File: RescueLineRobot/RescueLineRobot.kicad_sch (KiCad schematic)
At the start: 18 parts

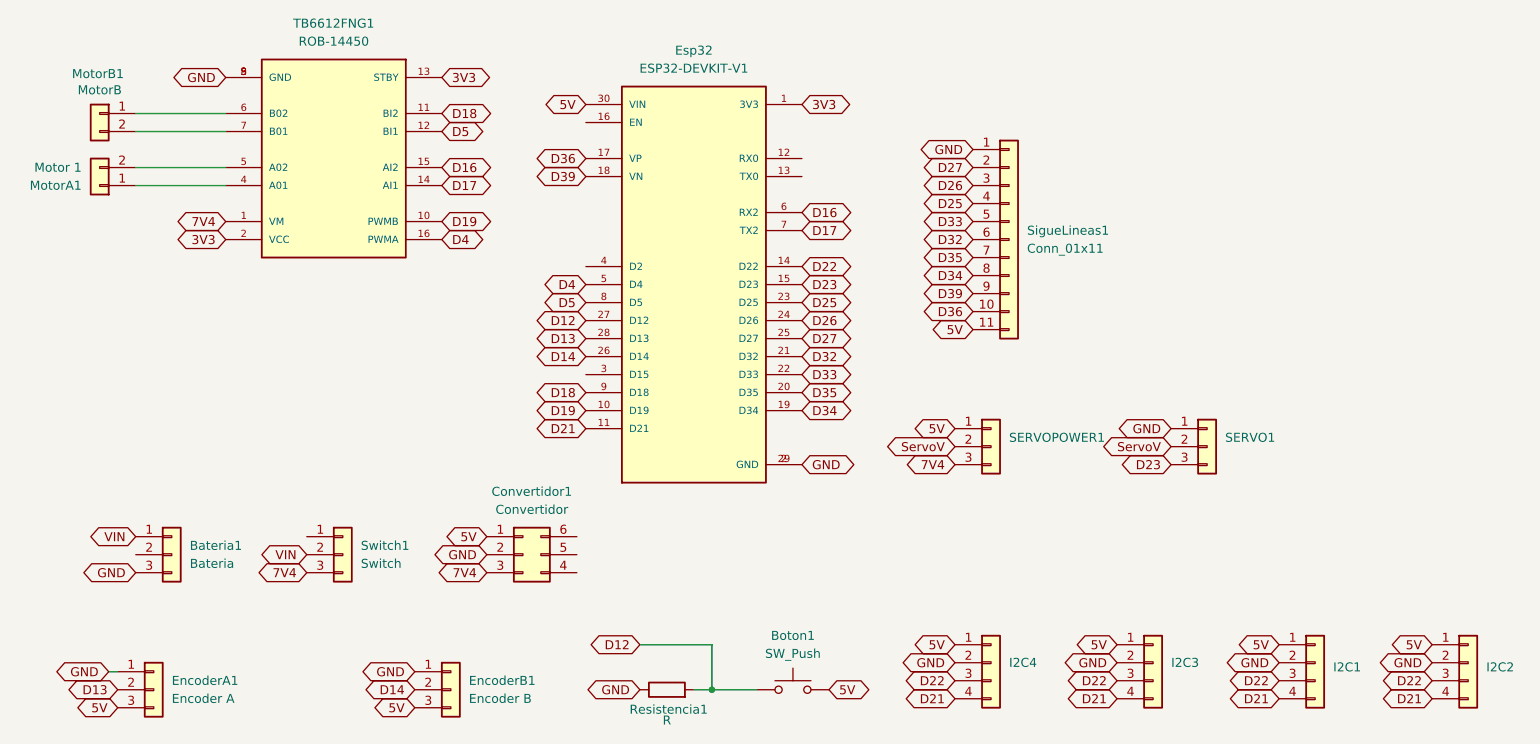
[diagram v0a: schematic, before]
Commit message: Cambio giroscopio
Se cambio el sistema de acople del giroscopio para que sea igual al del conversor de voltaje
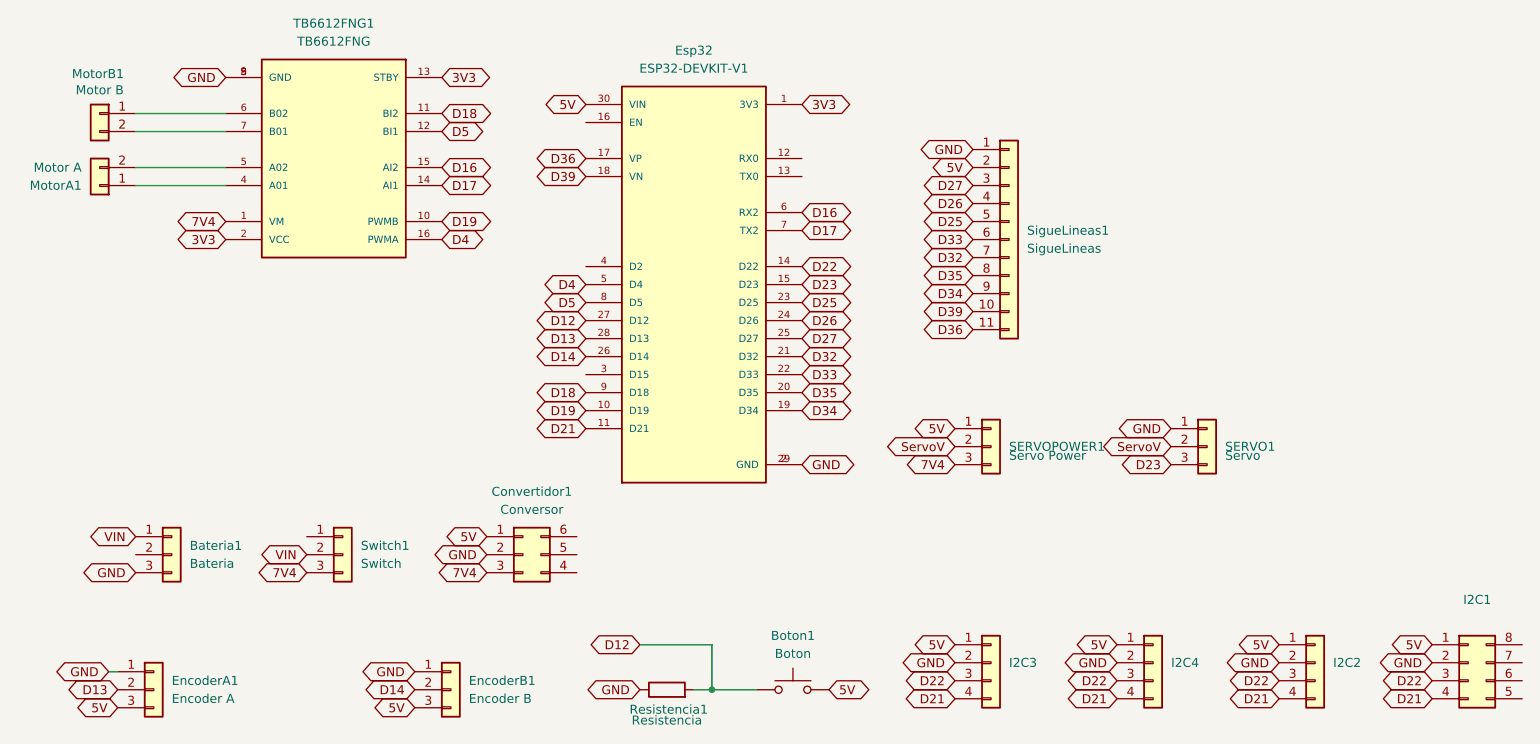
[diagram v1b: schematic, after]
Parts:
- Boton1: value SW_Push -> Boton
- Convertidor1: value Convertidor -> Conversor
- I2C1: renamed from I2C2; symbol Connector_Generic:Conn_01x04 -> Connector_Generic:Conn_02x04_Counter_Clockwise
- MotorA1: value Motor 1 -> Motor A
- MotorB1: value MotorB -> Motor B
- Resistencia1: value R -> Resistencia
- SERVO1: value Conn_01x03 -> Servo
- SERVOPOWER1: value Conn_01x03 -> Servo Power
- SigueLineas1: value Conn_01x11 -> SigueLineas
- TB6612FNG1: value ROB-14450 -> TB6612FNG
- renumbered I2C1 to I2C2, I2C4 to I2C3, I2C3 to I2C4
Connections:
- net 5V: now also SigueLineas1.2 (Pin_2); no longer SigueLineas1.11 (Pin_11)
- net D25: now also SigueLineas1.5 (Pin_5); no longer SigueLineas1.4 (Pin_4)
- net D26: now also SigueLineas1.4 (Pin_4); no longer SigueLineas1.3 (Pin_3)
- net D27: now also SigueLineas1.3 (Pin_3); no longer SigueLineas1.2 (Pin_2)
- net D32: now also SigueLineas1.7 (Pin_7); no longer SigueLineas1.6 (Pin_6)
- net D33: now also SigueLineas1.6 (Pin_6); no longer SigueLineas1.5 (Pin_5)
- net D34: now also SigueLineas1.9 (Pin_9); no longer SigueLineas1.8 (Pin_8)
- net D35: now also SigueLineas1.8 (Pin_8); no longer SigueLineas1.7 (Pin_7)
- net D36: now also SigueLineas1.11 (Pin_11); no longer SigueLineas1.10 (Pin_10)
- net D39: now also SigueLineas1.10 (Pin_10); no longer SigueLineas1.9 (Pin_9)
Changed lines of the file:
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@@
 	(global_label "D25"
 		(shape bidirectional)
-		(at 149.86 44.45 180)
+		(at 149.86 46.99 180)
 		(fields_autoplaced yes)
 		(effects
@@
 		)
 		(property "Intersheetrefs" "${INTERSHEET_REFS}"
-			(at 142.0745 44.45 0)
+			(at 142.0745 46.99 0)
 			(effects
 				(font
@@
 	(global_label "D27"
 		(shape bidirectional)
-		(at 149.86 39.37 180)
+		(at 149.86 41.91 180)
 		(fields_autoplaced yes)
 		(effects
@@
 		)
 		(property "Intersheetrefs" "${INTERSHEET_REFS}"
-			(at 142.0745 39.37 0)
+			(at 142.0745 41.91 0)
 			(effects
 				(font
@@
 	(global_label "D39"
 		(shape bidirectional)
-		(at 149.86 57.15 180)
+		(at 149.86 59.69 180)
 		(fields_autoplaced yes)
 		(effects
@@
 		)
 		(property "Intersheetrefs" "${INTERSHEET_REFS}"
-			(at 142.0745 57.15 0)
+			(at 142.0745 59.69 0)
 			(effects
 				(font
@@
 	(global_label "5V"
 		(shape bidirectional)
-		(at 149.86 62.23 180)
+		(at 149.86 39.37 180)
 		(fields_autoplaced yes)
 		(effects
@@
 		)
 		(property "Intersheetrefs" "${INTERSHEET_REFS}"
-			(at 143.4654 62.23 0)
+			(at 143.4654 39.37 0)
 			(effects
 				(font
@@
 	(global_label "D33"
 		(shape bidirectional)
-		(at 149.86 46.99 180)
+		(at 149.86 49.53 180)
 		(fields_autoplaced yes)
 		(effects
@@
 		)
 		(property "Intersheetrefs" "${INTERSHEET_REFS}"
-			(at 142.0745 46.99 0)
+			(at 142.0745 49.53 0)
 			(effects
 				(font
@@
 	(global_label "D35"
 		(shape bidirectional)
-		(at 149.86 52.07 180)
+		(at 149.86 54.61 180)
 		(fields_autoplaced yes)
 		(effects
@@
 		)
 		(property "Intersheetrefs" "${INTERSHEET_REFS}"
-			(at 142.0745 52.07 0)
+			(at 142.0745 54.61 0)
 			(effects
 				(font
@@
 	(global_label "D32"
 		(shape bidirectional)
-		(at 149.86 49.53 180)
+		(at 149.86 52.07 180)
 		(fields_autoplaced yes)
 		(effects
@@
 		)
 		(property "Intersheetrefs" "${INTERSHEET_REFS}"
-			(at 142.0745 49.53 0)
+			(at 142.0745 52.07 0)
 			(effects
 				(font
@@
 	(global_label "D26"
 		(shape bidirectional)
-		(at 149.86 41.91 180)
+		(at 149.86 44.45 180)
 		(fields_autoplaced yes)
 		(effects
@@
 		)
 		(property "Intersheetrefs" "${INTERSHEET_REFS}"
-			(at 142.0745 41.91 0)
+			(at 142.0745 44.45 0)
 			(effects
 				(font
@@
 	(global_label "D34"
 		(shape bidirectional)
-		(at 149.86 54.61 180)
+		(at 149.86 57.15 180)
 		(fields_autoplaced yes)
 		(effects
@@
 		)
 		(property "Intersheetrefs" "${INTERSHEET_REFS}"
-			(at 142.0745 54.61 0)
+			(at 142.0745 57.15 0)
 			(effects
 				(font
@@
 	(global_label "D36"
 		(shape bidirectional)
-		(at 149.86 59.69 180)
+		(at 149.86 62.23 180)
 		(fields_autoplaced yes)
 		(effects
@@
 		)
 		(property "Intersheetrefs" "${INTERSHEET_REFS}"
-			(at 142.0745 59.69 0)
+			(at 142.0745 62.23 0)
 			(effects
 				(font
@@
 		(fields_autoplaced yes)
 		(property "Reference" "SERVO1"
-			(at 185.42 77.4699 0)
+			(at 185.42 78.7399 0)
 			(effects
 				(font
@@
 			)
 		)
-		(property "Value" "Conn_01x03"
+		(property "Value" "Servo"
 			(at 185.42 80.0099 0)
 			(effects
@@
 				)
 				(justify left)
-				(hide yes)
 			)
 		)
@@
 		(dnp no)
 		(fields_autoplaced yes)
-		(property "Reference" "I2C3"
+		(property "Reference" "I2C4"
 			(at 177.8 109.2199 0)
 			(effects
@@
 			(project "RescueLineRobot"
 				(path "/08dd59d3-3158-43a6-a3e1-925f8e86ce81"
-					(reference "I2C3")
+					(reference "I2C4")
 					(unit 1)
 				)
@@
 			)
 		)
-		(property "Value" "MotorB"
+		(property "Value" "Motor B"
 			(at 26.67 28.448 0)
 			(effects
@@
 		(dnp no)
 		(fields_autoplaced yes)
-		(property "Reference" "I2C4"
+		(property "Reference" "I2C3"
 			(at 154.94 109.2199 0)
 			(effects
@@
 			(project "RescueLineRobot"
 				(path "/08dd59d3-3158-43a6-a3e1-925f8e86ce81"
-					(reference "I2C4")
+					(reference "I2C3")
 					(unit 1)
 				)
@@
 		(dnp no)
 		(fields_autoplaced yes)
-		(property "Reference" "I2C1"
-			(at 200.66 109.8549 0)
+		(property "Reference" "I2C2"
+			(at 200.66 109.2199 0)
 			(effects
 				(font
@@
 		)
 		(property "Value" "~"
-			(at 200.66 111.76 0)
+			(at 200.66 111.7599 0)
 			(effects
 				(font
@@
 			(project "RescueLineRobot"
 				(path "/08dd59d3-3158-43a6-a3e1-925f8e86ce81"
-					(reference "I2C1")
+					(reference "I2C2")
 					(unit 1)
 				)
@@
 			)
 		)
-		(property "Value" "ROB-14450"
+		(property "Value" "TB6612FNG"
 			(at 59.69 21.59 0)
 			(effects
@@
 			)
 		)
-		(property "Value" "SW_Push"
+		(property "Value" "Boton"
 			(at 124.46 107.95 0)
 			(effects
@@
 			)
 		)
-		(property "Value" "Convertidor"
+		(property "Value" "Conversor"
 			(at 87.63 87.63 0)
 			(effects
@@
 	)
 	(symbol
-		(lib_id "Connector_Generic:Conn_01x04")
+		(lib_id "Connector_Generic:Conn_02x04_Counter_Clockwise")
 		(at 219.71 109.22 0)
 		(unit 1)
@@
 		(dnp no)
 		(fields_autoplaced yes)
-		(property "Reference" "I2C2"
-			(at 222.25 109.8549 0)
+		(property "Reference" "I2C1"
+			(at 220.98 100.33 0)
 			(effects
 				(font
 					(size 1.27 1.27)
 				)
-				(justify left)
 			)
 		)
 		(property "Value" "~"
-			(at 222.25 111.76 0)
+			(at 220.98 102.87 0)
 			(effects
 				(font
 					(size 1.27 1.27)
 				)
-				(justify left)
 			)
 		)
@@
 			)
 		)
-		(property "Description" "Generic connector, single row, 01x04, script generated (kicad-library-utils/schlib/autogen/connector/)"
+		(property "Description" "Generic connector, double row, 02x04, counter clockwise pin numbering scheme (similar to DIP package numbering), script generated (kicad-library-utils/schlib/autogen/connector/)"
 			(at 219.71 109.22 0)
 			(effects
@@
 		(pin "4"
 		)
+		(pin "8"
+		)
+		(pin "7"
+		)
+		(pin "6"
+		)
+		(pin "5"
+		)
 		(instances
 			(project "RescueLineRobot"
 				(path "/08dd59d3-3158-43a6-a3e1-925f8e86ce81"
-					(reference "I2C2")
+					(reference "I2C1")
 					(unit 1)
 				)
@@
 			)
 		)
-		(property "Value" "Motor 1"
+		(property "Value" "Motor A"
 			(at 24.13 39.3701 0)
 			(effects
@@
 		(fields_autoplaced yes)
 		(property "Reference" "SERVOPOWER1"
-			(at 154.94 77.4699 0)
+			(at 154.94 78.7399 0)
 			(effects
 				(font
@@
 			)
 		)
-		(property "Value" "Conn_01x03"
+		(property "Value" "Servo Power"
 			(at 154.94 80.0099 0)
 			(effects
@@
 				)
 				(justify left)
-				(hide yes)
 			)
 		)
@@
 			)
 		)
-		(property "Value" "R"
+		(property "Value" "Resistencia"
 			(at 106.68 117.348 90)
 			(effects
@@
 			)
 		)
-		(property "Value" "Conn_01x11"
+		(property "Value" "SigueLineas"
 			(at 157.48 50.7999 0)
 			(effects

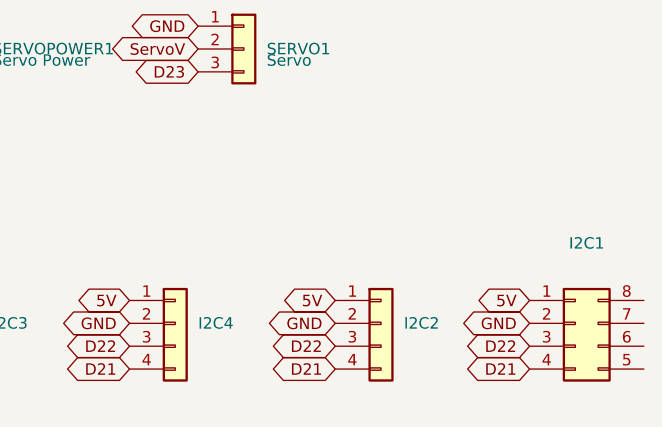
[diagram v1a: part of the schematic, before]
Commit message: Last pcb changes
Arreglo de puerto i2c para el giroscopio
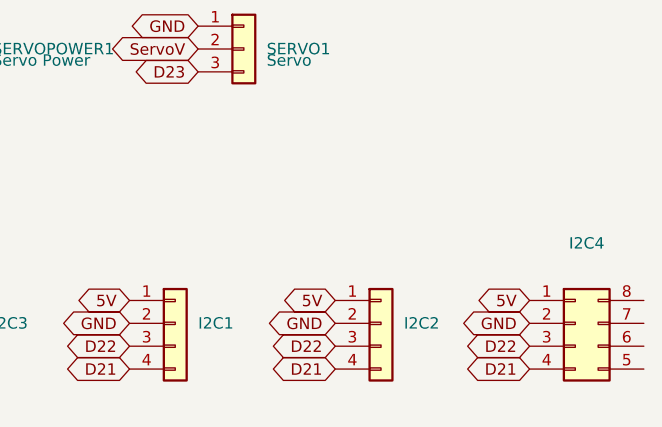
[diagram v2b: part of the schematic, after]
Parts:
- renumbered I2C4 to I2C1, I2C1 to I2C4
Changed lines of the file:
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@@
 		(dnp no)
 		(fields_autoplaced yes)
-		(property "Reference" "I2C4"
+		(property "Reference" "I2C1"
 			(at 177.8 109.2199 0)
 			(effects
@@
 			(project "RescueLineRobot"
 				(path "/08dd59d3-3158-43a6-a3e1-925f8e86ce81"
-					(reference "I2C4")
+					(reference "I2C1")
 					(unit 1)
 				)
@@
 		(dnp no)
 		(fields_autoplaced yes)
-		(property "Reference" "I2C1"
+		(property "Reference" "I2C4"
 			(at 220.98 100.33 0)
 			(effects
@@
 			(project "RescueLineRobot"
 				(path "/08dd59d3-3158-43a6-a3e1-925f8e86ce81"
-					(reference "I2C1")
-					(unit 1)
-				)
+					(reference "I2C4")
+					(unit 1)
+				)
